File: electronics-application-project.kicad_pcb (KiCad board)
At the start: 2 copper layers, 65 x 51.5 mm, 53 parts, among them J1 Conn_02x03_Odd_Even, J2 Conn_01x02_Pin, J3 Conn_01x02_Pin, J4 Conn_01x02_Pin, U1 W5500, U2 ARJM11C7-114-BA-EW2, U3 LM2574-3.3YN, U4 ATTINY85-20SU, U5 74HC00, Y2 ABLS7M2-25.000MHZ-D-2Y-T

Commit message: DRC pass
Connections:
- J1 pad 4: /MISO -> /MOSI
- J1 pad 8: /MOSI -> /MISO
- U4 pad 2: /MOSI -> /MISO
- U4 pad 5: /MISO -> /MOSI
- U5 pad 13: /MISO -> /MOSI
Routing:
- net /MISO: track 36.7 -> 26.5 mm, vias 1 -> 2
- net /MOSI: track 33.1 -> 36.8 mm, vias 4 -> 2
- net /SCSn: track 58.1 -> 61.1 mm
- net 3.3V_D: track 196.7 -> 196.9 mm, vias 3 -> 2

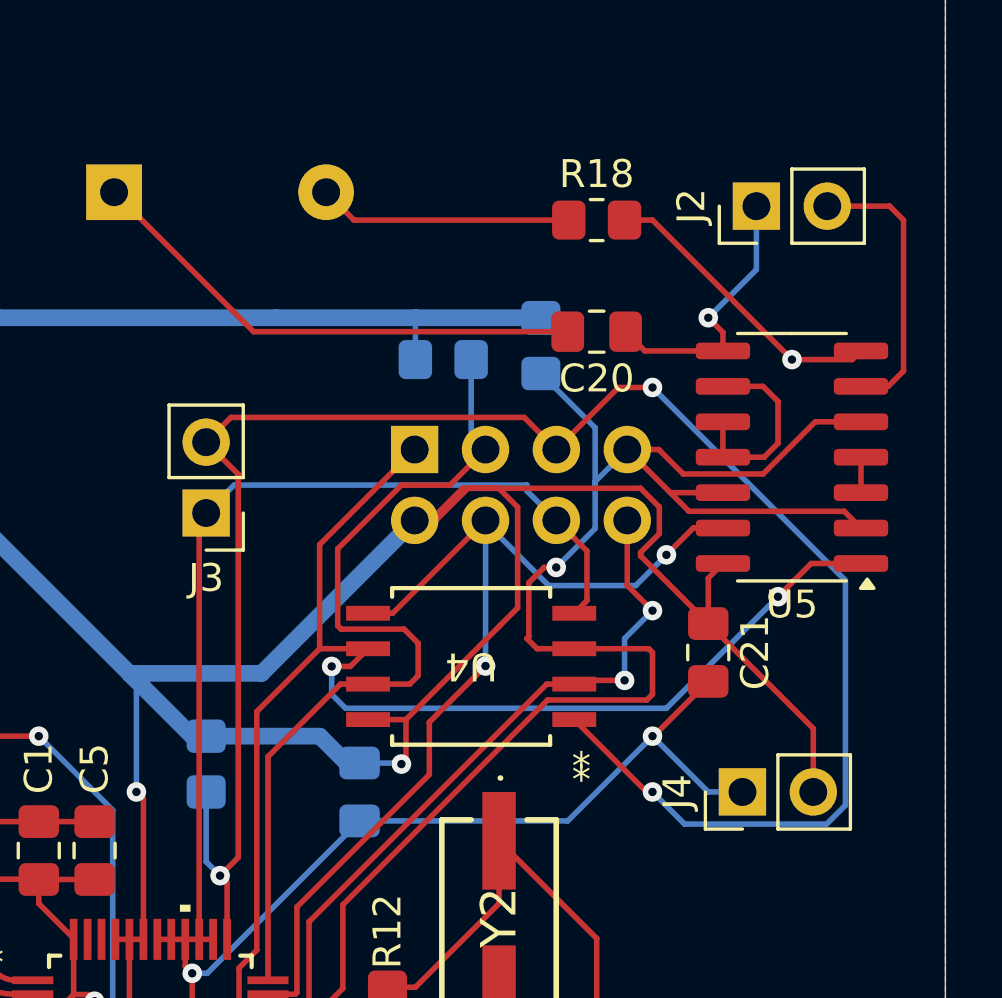
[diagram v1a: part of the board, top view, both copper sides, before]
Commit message: remove redundant header from layout
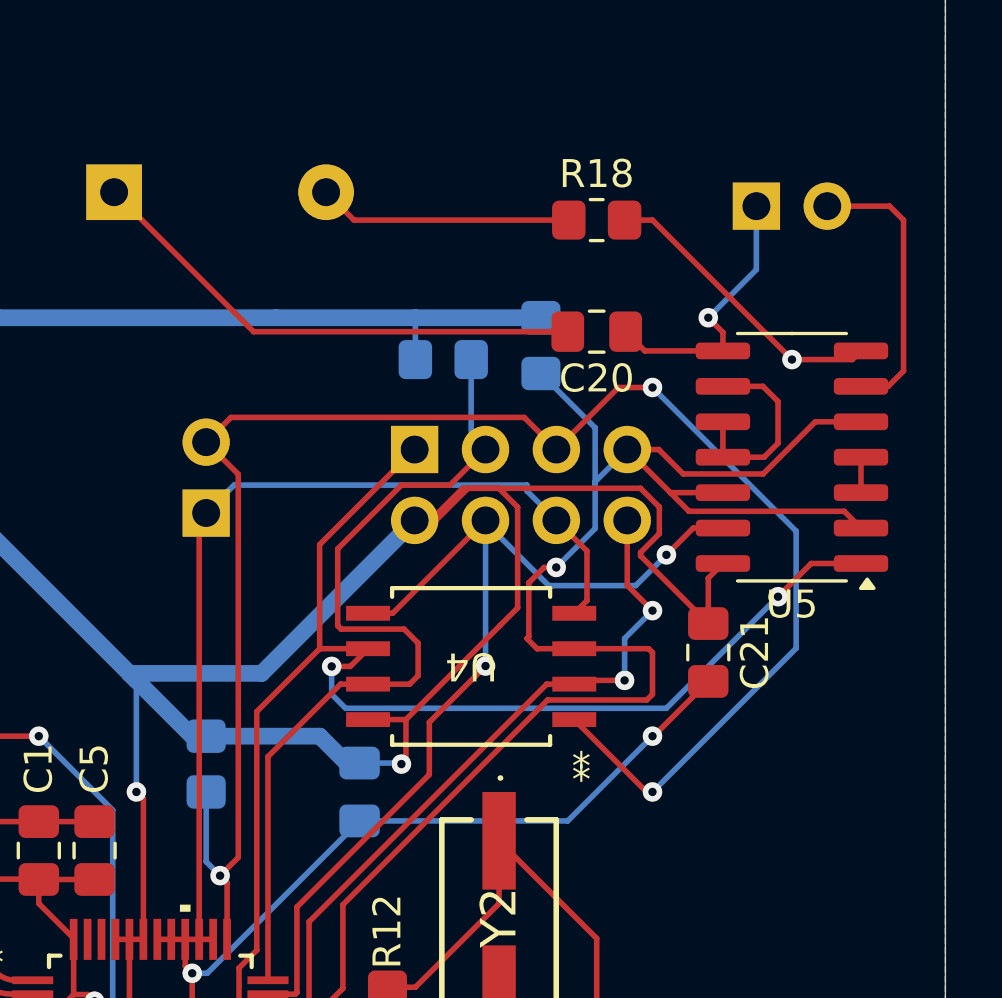
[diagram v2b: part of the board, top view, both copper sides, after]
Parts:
- removed J4: Conn_01x02_Pin, Connector_PinHeader_2.54mm:PinHeader_1x02_P2.54mm_Vertical
- J2, J3: moved to B.Cu
- turned J2 to -90 degrees
- turned J3 to 0 degrees
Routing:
- net 3.3V_D: track 196.9 -> 189.3 mm
- net /RSTn: track 69.0 -> 62.3 mm
- net GND: track 199.1 -> 195.0 mm

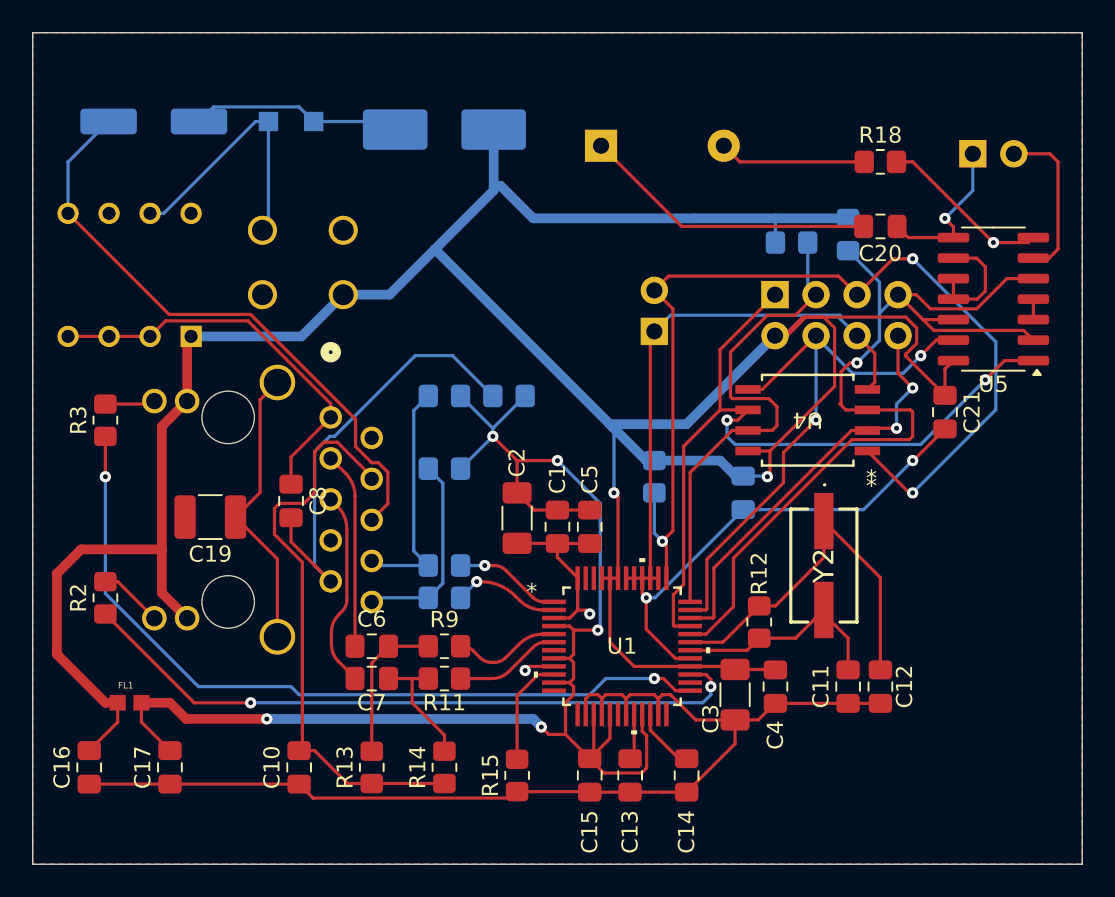
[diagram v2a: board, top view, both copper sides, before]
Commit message: shrinking of the board
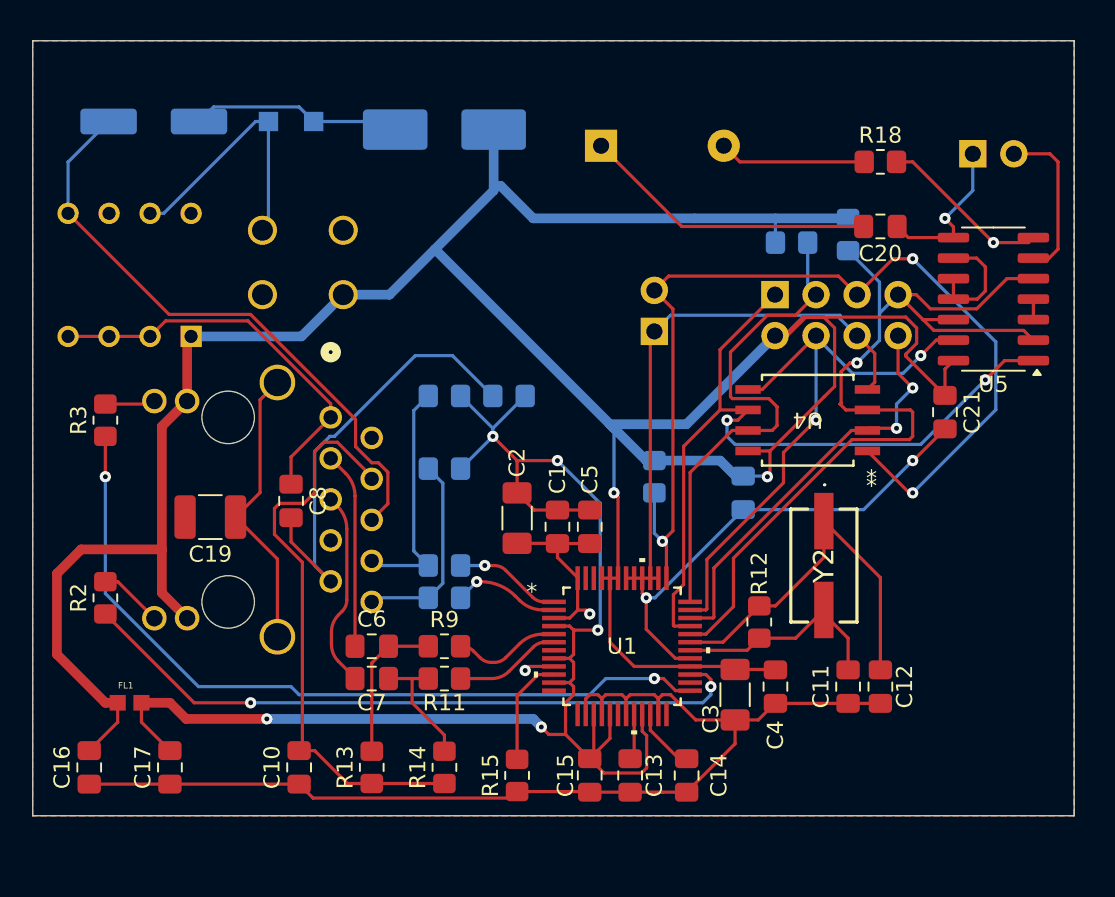
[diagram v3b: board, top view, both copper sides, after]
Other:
- board size 65 x 51.5 mm -> 64.5 x 48 mm
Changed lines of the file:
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@@
 		(tags "capacitor handsolder")
 		(property "Reference" "C15"
-			(at -3.5 0 90)
+			(at 0 -1.5 90)
 			(layer "F.SilkS")
 			(effects
@@
 		(tags "capacitor handsolder")
 		(property "Reference" "C14"
-			(at -3.5 0 90)
+			(at 0 2 90)
 			(layer "F.SilkS")
 			(effects
@@
 		(tags "capacitor handsolder")
 		(property "Reference" "C13"
-			(at -3.5 0 90)
+			(at 0 1.5 90)
 			(layer "F.SilkS")
 			(effects
@@
 		(tags "capacitor electrolytic")
 		(property "Reference" "C9"
-			(at 0 5.2 0)
+			(at 0 -5 0)
 			(layer "B.SilkS")
 			(effects
@@
 	)
 	(gr_rect
-		(start 115.5 76.5)
-		(end 180.5 128)
+		(start 115.5 77)
+		(end 180 125)
 		(stroke
 			(width 0.05)
@@
 		(layer "F.Cu")
 		(pts
-			(xy 115.5 76.5) (xy 180.5 76.5)
+			(xy 115.5 77) (xy 180 77)
 		)
-		(height -3.5)
+		(height -5.5)
 		(orientation 0)
 		(format
@@
 			(keep_text_aligned yes)
 		)
-		(gr_text "65.0000 mm"
-			(at 148 71.2 0)
+		(gr_text "64,5000 mm"
+			(at 147.75 69.7 0)
 			(layer "F.Cu")
 			(effects
@@
 		(layer "F.Cu")
 		(pts
-			(xy 115.5 76.5) (xy 115.5 128)
+			(xy 115.5 77) (xy 115.5 125)
 		)
-		(height -5)
+		(height -6)
 		(orientation 1)
 		(format
@@
 			(keep_text_aligned yes)
 		)
-		(gr_text "51.5000 mm"
-			(at 108.7 102.25 90)
+		(gr_text "48,0000 mm"
+			(at 107.7 101 90)
 			(layer "F.Cu")
 			(effects
@@
 		(polygon
 			(pts
-				(xy 115.5 76.5) (xy 180.5 76.5) (xy 180.5 128) (xy 115.5 128)
+				(xy 115.5 77) (xy 180 77) (xy 180 125) (xy 115.5 125)
 			)
 		)

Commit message: ship it
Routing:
- net Net-(U2-VC2+): track 37.5 -> 43.2 mm
- net 3.3V_D: track 189.3 -> 187.4 mm
